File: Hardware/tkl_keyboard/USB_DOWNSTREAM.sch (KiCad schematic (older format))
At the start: 2 parts, among them J2 USB_C_Receptacle_USB2.0

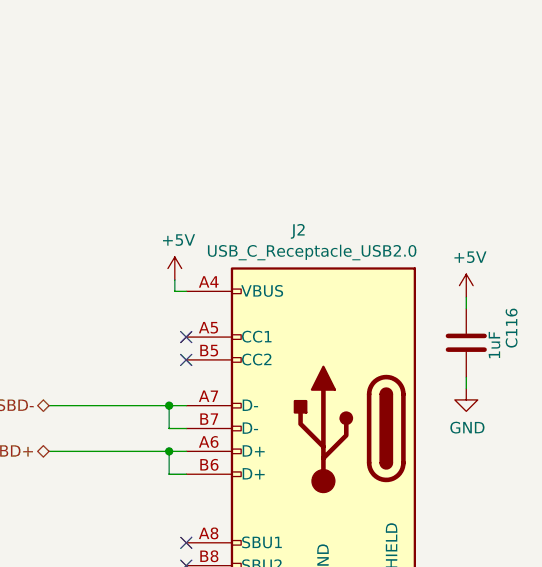
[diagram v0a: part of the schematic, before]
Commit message: Keyswitch, LED and diode placement done
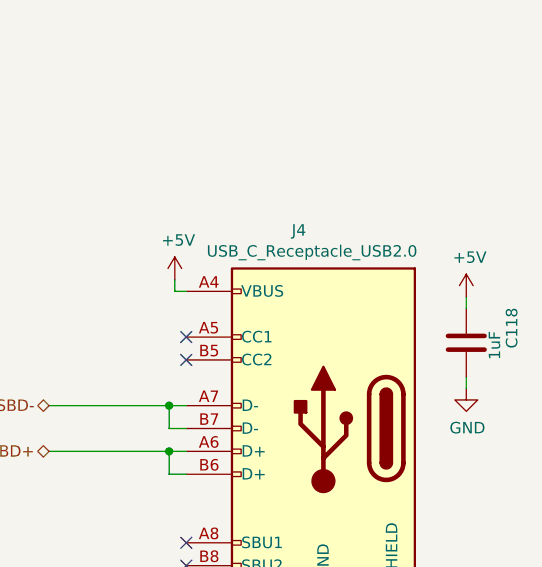
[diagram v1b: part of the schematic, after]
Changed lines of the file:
@@
 AR Path="/6511E0C5/651136DD" Ref="J3"  Part="1"
 AR Path="/65128D7D/651136DD" Ref="J4"  Part="1"
-F 0 "J2" H 6257 4567 50  0000 C CNN
+F 0 "J4" H 6257 4567 50  0000 C CNN
 F 1 "USB_C_Receptacle_USB2.0" H 6200 4475 50  0000 C CNN
 F 2 "Connector_USB:USB_C_Receptacle_GCT_USB4085" H 6300 3700 50  0001 C CNN
@@
 AR Path="/6511E0C5/651136EF" Ref="#PWR0497"  Part="1"
 AR Path="/65128D7D/651136EF" Ref="#PWR0501"  Part="1"
-F 0 "#PWR0493" H 6575 4425 50  0001 C CNN
+F 0 "#PWR0501" H 6575 4425 50  0001 C CNN
 F 1 "GND" H 6580 4502 50  0000 C CNN
 F 2 "" H 6575 4675 50  0001 C CNN
@@
 AR Path="/6511E0C5/651136FD" Ref="#PWR0496"  Part="1"
 AR Path="/65128D7D/651136FD" Ref="#PWR0500"  Part="1"
-F 0 "#PWR0492" H 5500 2900 50  0001 C CNN
+F 0 "#PWR0500" H 5500 2900 50  0001 C CNN
 F 1 "+5V" H 5515 3223 50  0000 C CNN
 F 2 "" H 5500 3050 50  0001 C CNN
@@
 AR Path="/6511E0C5/65113705" Ref="C117"  Part="1"
 AR Path="/65128D7D/65113705" Ref="C118"  Part="1"
-F 0 "C116" V 6975 3300 50  0000 L CNN
+F 0 "C118" V 6975 3300 50  0000 L CNN
 F 1 "1uF" V 6900 3250 50  0000 L CNN
 F 2 "Capacitor_smd:C_0603_1608Metric" H 6813 3175 50  0001 C CNN
@@
 AR Path="/6511E0C5/6511370B" Ref="#PWR0498"  Part="1"
 AR Path="/65128D7D/6511370B" Ref="#PWR0502"  Part="1"
-F 0 "#PWR0494" H 6775 2975 50  0001 C CNN
+F 0 "#PWR0502" H 6775 2975 50  0001 C CNN
 F 1 "+5V" H 6790 3298 50  0000 C CNN
 F 2 "" H 6775 3125 50  0001 C CNN
@@
 AR Path="/6511E0C5/65113712" Ref="#PWR0499"  Part="1"
 AR Path="/65128D7D/65113712" Ref="#PWR0503"  Part="1"
-F 0 "#PWR0495" H 6775 3275 50  0001 C CNN
+F 0 "#PWR0503" H 6775 3275 50  0001 C CNN
 F 1 "GND" H 6780 3352 50  0000 C CNN
 F 2 "" H 6775 3525 50  0001 C CNN

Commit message: LEDs and diodes routed
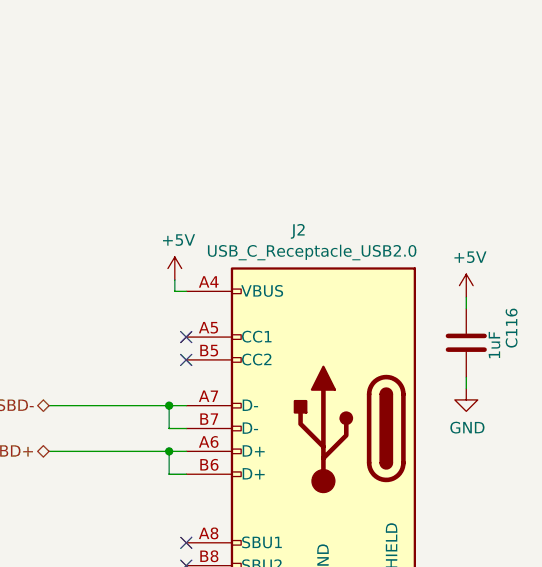
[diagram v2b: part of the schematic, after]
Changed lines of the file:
@@
 AR Path="/6511E0C5/651136DD" Ref="J3"  Part="1"
 AR Path="/65128D7D/651136DD" Ref="J4"  Part="1"
-F 0 "J4" H 6257 4567 50  0000 C CNN
+F 0 "J2" H 6257 4567 50  0000 C CNN
 F 1 "USB_C_Receptacle_USB2.0" H 6200 4475 50  0000 C CNN
 F 2 "Connector_USB:USB_C_Receptacle_GCT_USB4085" H 6300 3700 50  0001 C CNN
@@
 AR Path="/6511E0C5/65113705" Ref="C117"  Part="1"
 AR Path="/65128D7D/65113705" Ref="C118"  Part="1"
-F 0 "C118" V 6975 3300 50  0000 L CNN
+F 0 "C116" V 6975 3300 50  0000 L CNN
 F 1 "1uF" V 6900 3250 50  0000 L CNN
 F 2 "Capacitor_smd:C_0603_1608Metric" H 6813 3175 50  0001 C CNN

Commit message: Rows and columns routed to controller. Extended top board edge to fit OLED. Removed optional resistors around CMC.
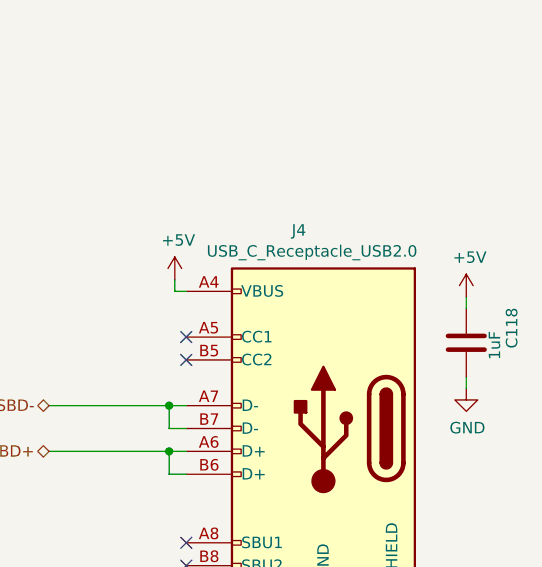
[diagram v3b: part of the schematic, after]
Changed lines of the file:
@@
 $Descr A4 11693 8268
 encoding utf-8
-Sheet 8 11
+Sheet 11 11
 Title ""
 Date ""
@@
 AR Path="/6511E0C5/651136DD" Ref="J3"  Part="1"
 AR Path="/65128D7D/651136DD" Ref="J4"  Part="1"
-F 0 "J2" H 6257 4567 50  0000 C CNN
+F 0 "J4" H 6257 4567 50  0000 C CNN
 F 1 "USB_C_Receptacle_USB2.0" H 6200 4475 50  0000 C CNN
 F 2 "Connector_USB:USB_C_Receptacle_GCT_USB4085" H 6300 3700 50  0001 C CNN
@@
 AR Path="/6511E0C5/65113705" Ref="C117"  Part="1"
 AR Path="/65128D7D/65113705" Ref="C118"  Part="1"
-F 0 "C116" V 6975 3300 50  0000 L CNN
+F 0 "C118" V 6975 3300 50  0000 L CNN
 F 1 "1uF" V 6900 3250 50  0000 L CNN
 F 2 "Capacitor_smd:C_0603_1608Metric" H 6813 3175 50  0001 C CNN

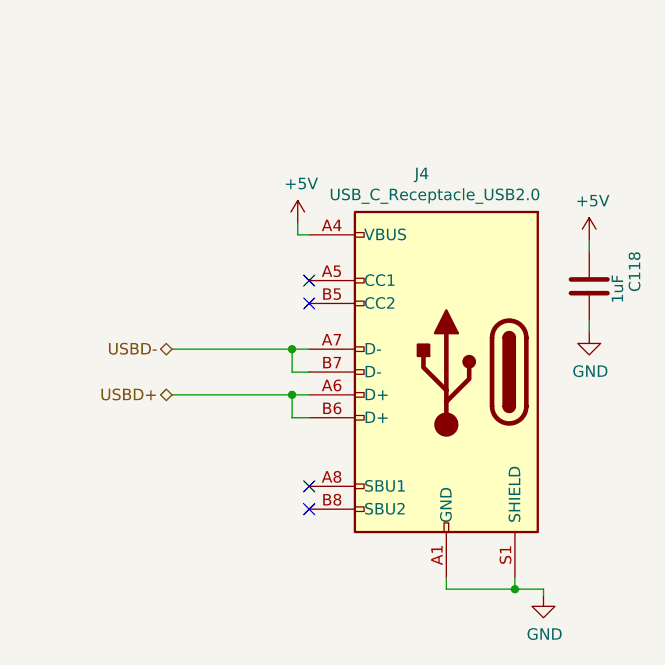
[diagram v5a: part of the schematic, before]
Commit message: Fixing USB circuit, adding data line resistors as per AN-5052
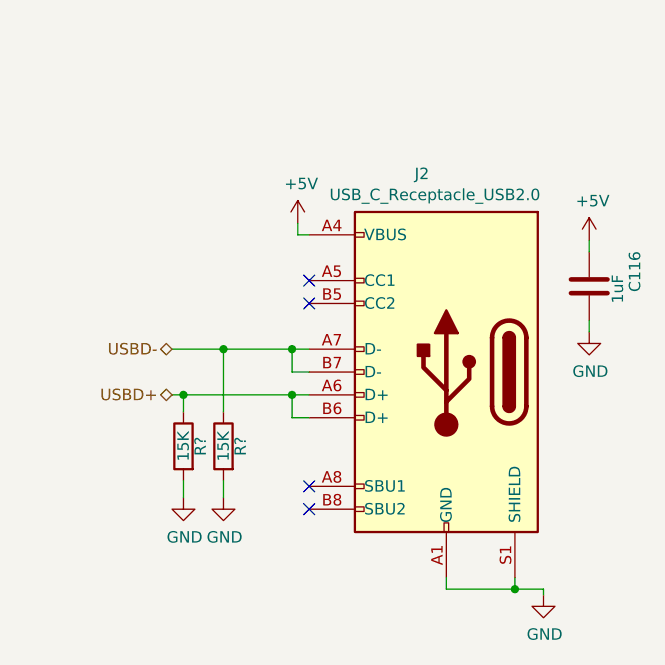
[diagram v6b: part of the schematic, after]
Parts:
- added R? (x2): 15K, resistor_smd:R_0603_1608Metric, symbol Device:R
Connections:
- net GND: now also R?.2, R?.2
- net USBD+: now also R?.1
- net USBD-: now also R?.1
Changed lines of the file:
@@
 $Descr A4 11693 8268
 encoding utf-8
-Sheet 11 12
+Sheet 8 12
 Title ""
 Date ""
@@
 AR Path="/6511E0C5/651136DD" Ref="J3"  Part="1"
 AR Path="/65128D7D/651136DD" Ref="J4"  Part="1"
-F 0 "J4" H 6257 4567 50  0000 C CNN
+F 0 "J2" H 6257 4567 50  0000 C CNN
 F 1 "USB_C_Receptacle_USB2.0" H 6200 4475 50  0000 C CNN
 F 2 "Connector_USB:USB_C_Receptacle_GCT_USB4085" H 6300 3700 50  0001 C CNN
@@
 	5475 3600 5550 3600
 Wire Wire Line
-	4950 3600 5475 3600
+	4950 3600 5175 3600
 Connection ~ 5475 3600
 Wire Wire Line
-	4950 3800 5475 3800
+	4950 3800 5000 3800
 Connection ~ 5475 3800
 NoConn ~ 5550 4200
@@
 AR Path="/6511E0C5/651136EF" Ref="#PWR0497"  Part="1"
 AR Path="/65128D7D/651136EF" Ref="#PWR0501"  Part="1"
-F 0 "#PWR0501" H 6575 4425 50  0001 C CNN
+F 0 "#PWR0493" H 6575 4425 50  0001 C CNN
 F 1 "GND" H 6580 4502 50  0000 C CNN
 F 2 "" H 6575 4675 50  0001 C CNN
@@
 AR Path="/6511E0C5/651136FD" Ref="#PWR0496"  Part="1"
 AR Path="/65128D7D/651136FD" Ref="#PWR0500"  Part="1"
-F 0 "#PWR0500" H 5500 2900 50  0001 C CNN
+F 0 "#PWR0492" H 5500 2900 50  0001 C CNN
 F 1 "+5V" H 5515 3223 50  0000 C CNN
 F 2 "" H 5500 3050 50  0001 C CNN
@@
 AR Path="/6511E0C5/65113705" Ref="C117"  Part="1"
 AR Path="/65128D7D/65113705" Ref="C118"  Part="1"
-F 0 "C118" V 6975 3300 50  0000 L CNN
+F 0 "C116" V 6975 3300 50  0000 L CNN
 F 1 "1uF" V 6900 3250 50  0000 L CNN
 F 2 "Capacitor_smd:C_0603_1608Metric" H 6813 3175 50  0001 C CNN
@@
 AR Path="/6511E0C5/6511370B" Ref="#PWR0498"  Part="1"
 AR Path="/65128D7D/6511370B" Ref="#PWR0502"  Part="1"
-F 0 "#PWR0502" H 6775 2975 50  0001 C CNN
+F 0 "#PWR0494" H 6775 2975 50  0001 C CNN
 F 1 "+5V" H 6790 3298 50  0000 C CNN
 F 2 "" H 6775 3125 50  0001 C CNN
@@
 AR Path="/6511E0C5/65113712" Ref="#PWR0499"  Part="1"
 AR Path="/65128D7D/65113712" Ref="#PWR0503"  Part="1"
-F 0 "#PWR0503" H 6775 3275 50  0001 C CNN
+F 0 "#PWR0495" H 6775 3275 50  0001 C CNN
 F 1 "GND" H 6780 3352 50  0000 C CNN
 F 2 "" H 6775 3525 50  0001 C CNN
@@
 Text HLabel 4950 3800 0    50   BiDi ~ 0
 USBD+
+$Comp
+L Device:R R?
+U 1 1 614BD77F
+P 5000 4025
+AR Path="/6114D32E/614BD77F" Ref="R?"  Part="1"
+AR Path="/6247A5CE/614BD77F" Ref="R?"  Part="1"
+AR Path="/61234350/614BD77F" Ref="R?"  Part="1"
+AR Path="/62FAC6FD/614BD77F" Ref="R?"  Part="1"
+AR Path="/650FF941/614BD77F" Ref="R?"  Part="1"
+AR Path="/6511E0C5/614BD77F" Ref="R?"  Part="1"
+AR Path="/65128D7D/614BD77F" Ref="R?"  Part="1"
+F 0 "R?" V 4925 4025 50  0000 C CNN
+F 1 "15K" V 5000 4025 50  0000 C CNN
+F 2 "resistor_smd:R_0603_1608Metric" V 4930 4025 50  0001 C CNN
+F 3 "~" H 5000 4025 50  0001 C CNN
+	1    5000 4025
+	-1   0    0    -1
+$EndComp
+$Comp
+L Device:R R?
+U 1 1 614BD896
+P 5175 4025
+AR Path="/6114D32E/614BD896" Ref="R?"  Part="1"
+AR Path="/6247A5CE/614BD896" Ref="R?"  Part="1"
+AR Path="/61234350/614BD896" Ref="R?"  Part="1"
+AR Path="/62FAC6FD/614BD896" Ref="R?"  Part="1"
+AR Path="/650FF941/614BD896" Ref="R?"  Part="1"
+AR Path="/6511E0C5/614BD896" Ref="R?"  Part="1"
+AR Path="/65128D7D/614BD896" Ref="R?"  Part="1"
+F 0 "R?" V 5100 4025 50  0000 C CNN
+F 1 "15K" V 5175 4025 50  0000 C CNN
+F 2 "resistor_smd:R_0603_1608Metric" V 5105 4025 50  0001 C CNN
+F 3 "~" H 5175 4025 50  0001 C CNN
+	1    5175 4025
+	-1   0    0    -1
+$EndComp
+Wire Wire Line
+	5000 3875 5000 3800
+Connection ~ 5000 3800
+Wire Wire Line
+	5000 3800 5475 3800
+Wire Wire Line
+	5175 3875 5175 3600
+Connection ~ 5175 3600
+Wire Wire Line
+	5175 3600 5475 3600
+$Comp
+L power:GND #PWR?
+U 1 1 614BE05C
+P 5000 4250
+AR Path="/6114D32E/614BE05C" Ref="#PWR?"  Part="1"
+AR Path="/6247A5CE/614BE05C" Ref="#PWR?"  Part="1"
+AR Path="/61234350/614BE05C" Ref="#PWR?"  Part="1"
+AR Path="/62FAC6FD/614BE05C" Ref="#PWR?"  Part="1"
+AR Path="/650FF941/614BE05C" Ref="#PWR?"  Part="1"
+AR Path="/6511E0C5/614BE05C" Ref="#PWR?"  Part="1"
+AR Path="/65128D7D/614BE05C" Ref="#PWR?"  Part="1"
+F 0 "#PWR?" H 5000 4000 50  0001 C CNN
+F 1 "GND" H 5005 4077 50  0000 C CNN
+F 2 "" H 5000 4250 50  0001 C CNN
+F 3 "" H 5000 4250 50  0001 C CNN
+	1    5000 4250
+	1    0    0    -1
+$EndComp
+$Comp
+L power:GND #PWR?
+U 1 1 614BE37F
+P 5175 4250
+AR Path="/6114D32E/614BE37F" Ref="#PWR?"  Part="1"
+AR Path="/6247A5CE/614BE37F" Ref="#PWR?"  Part="1"
+AR Path="/61234350/614BE37F" Ref="#PWR?"  Part="1"
+AR Path="/62FAC6FD/614BE37F" Ref="#PWR?"  Part="1"
+AR Path="/650FF941/614BE37F" Ref="#PWR?"  Part="1"
+AR Path="/6511E0C5/614BE37F" Ref="#PWR?"  Part="1"
+AR Path="/65128D7D/614BE37F" Ref="#PWR?"  Part="1"
+F 0 "#PWR?" H 5175 4000 50  0001 C CNN
+F 1 "GND" H 5180 4077 50  0000 C CNN
+F 2 "" H 5175 4250 50  0001 C CNN
+F 3 "" H 5175 4250 50  0001 C CNN
+	1    5175 4250
+	1    0    0    -1
+$EndComp
+Wire Wire Line
+	5000 4250 5000 4175
+Wire Wire Line
+	5175 4250 5175 4175
 $EndSCHEMATC

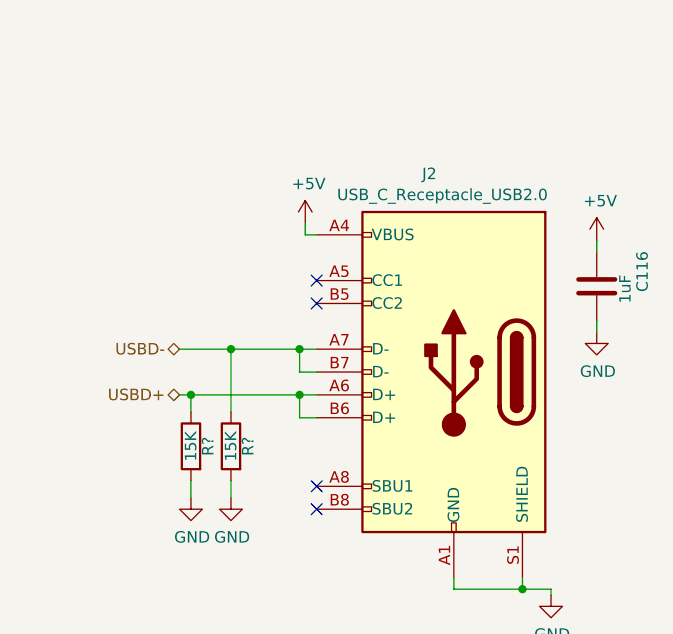
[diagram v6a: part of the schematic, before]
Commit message: Tidying schematic
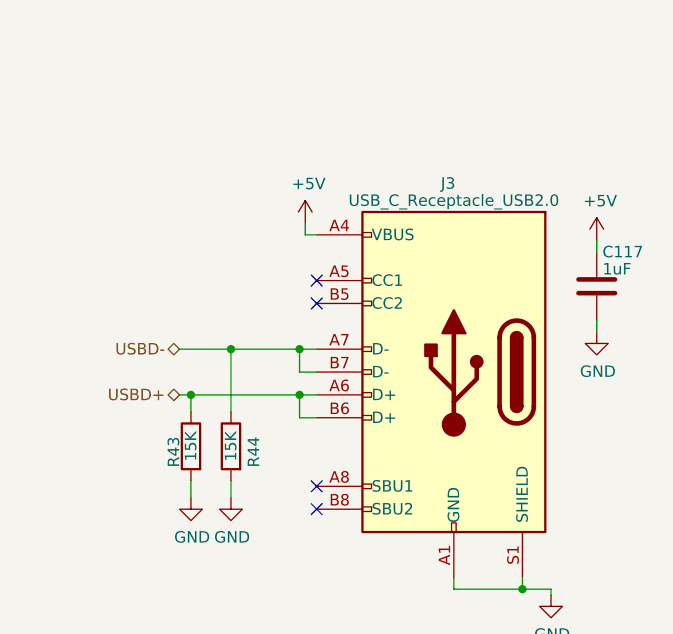
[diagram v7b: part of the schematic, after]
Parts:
- gave numbers to parts that had none: 2
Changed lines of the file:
@@
 $Descr A4 11693 8268
 encoding utf-8
-Sheet 8 12
-Title ""
+Sheet 10 12
+Title "TKL Keyboard"
 Date ""
-Rev ""
+Rev "0"
 Comp ""
 Comment1 ""
@@
 AR Path="/6511E0C5/651136DD" Ref="J3"  Part="1"
 AR Path="/65128D7D/651136DD" Ref="J4"  Part="1"
-F 0 "J2" H 6257 4567 50  0000 C CNN
-F 1 "USB_C_Receptacle_USB2.0" H 6200 4475 50  0000 C CNN
+F 0 "J3" H 6175 4525 50  0000 C CNN
+F 1 "USB_C_Receptacle_USB2.0" H 6150 4450 50  0000 C CNN
 F 2 "Connector_USB:USB_C_Receptacle_GCT_USB4085" H 6300 3700 50  0001 C CNN
 F 3 "https://www.usb.org/sites/default/files/documents/usb_type-c.zip" H 6300 3700 50  0001 C CNN
@@
 AR Path="/6511E0C5/651136EF" Ref="#PWR0497"  Part="1"
 AR Path="/65128D7D/651136EF" Ref="#PWR0501"  Part="1"
-F 0 "#PWR0493" H 6575 4425 50  0001 C CNN
+F 0 "#PWR0497" H 6575 4425 50  0001 C CNN
 F 1 "GND" H 6580 4502 50  0000 C CNN
 F 2 "" H 6575 4675 50  0001 C CNN
@@
 AR Path="/6511E0C5/651136FD" Ref="#PWR0496"  Part="1"
 AR Path="/65128D7D/651136FD" Ref="#PWR0500"  Part="1"
-F 0 "#PWR0492" H 5500 2900 50  0001 C CNN
+F 0 "#PWR0496" H 5500 2900 50  0001 C CNN
 F 1 "+5V" H 5515 3223 50  0000 C CNN
 F 2 "" H 5500 3050 50  0001 C CNN
@@
 AR Path="/6511E0C5/65113705" Ref="C117"  Part="1"
 AR Path="/65128D7D/65113705" Ref="C118"  Part="1"
-F 0 "C116" V 6975 3300 50  0000 L CNN
-F 1 "1uF" V 6900 3250 50  0000 L CNN
+F 0 "C117" H 6800 3475 50  0000 L CNN
+F 1 "1uF" H 6800 3400 50  0000 L CNN
 F 2 "Capacitor_smd:C_0603_1608Metric" H 6813 3175 50  0001 C CNN
 F 3 "~" H 6775 3325 50  0001 C CNN
@@
 AR Path="/6511E0C5/6511370B" Ref="#PWR0498"  Part="1"
 AR Path="/65128D7D/6511370B" Ref="#PWR0502"  Part="1"
-F 0 "#PWR0494" H 6775 2975 50  0001 C CNN
+F 0 "#PWR0498" H 6775 2975 50  0001 C CNN
 F 1 "+5V" H 6790 3298 50  0000 C CNN
 F 2 "" H 6775 3125 50  0001 C CNN
@@
 AR Path="/6511E0C5/65113712" Ref="#PWR0499"  Part="1"
 AR Path="/65128D7D/65113712" Ref="#PWR0503"  Part="1"
-F 0 "#PWR0495" H 6775 3275 50  0001 C CNN
+F 0 "#PWR0499" H 6775 3275 50  0001 C CNN
 F 1 "GND" H 6780 3352 50  0000 C CNN
 F 2 "" H 6775 3525 50  0001 C CNN
@@
 AR Path="/61234350/614BD77F" Ref="R?"  Part="1"
 AR Path="/62FAC6FD/614BD77F" Ref="R?"  Part="1"
-AR Path="/650FF941/614BD77F" Ref="R?"  Part="1"
-AR Path="/6511E0C5/614BD77F" Ref="R?"  Part="1"
-AR Path="/65128D7D/614BD77F" Ref="R?"  Part="1"
-F 0 "R?" V 4925 4025 50  0000 C CNN
+AR Path="/650FF941/614BD77F" Ref="R40"  Part="1"
+AR Path="/6511E0C5/614BD77F" Ref="R43"  Part="1"
+AR Path="/65128D7D/614BD77F" Ref="R45"  Part="1"
+F 0 "R43" V 5075 4000 50  0000 C CNN
 F 1 "15K" V 5000 4025 50  0000 C CNN
 F 2 "resistor_smd:R_0603_1608Metric" V 4930 4025 50  0001 C CNN
@@
 AR Path="/61234350/614BD896" Ref="R?"  Part="1"
 AR Path="/62FAC6FD/614BD896" Ref="R?"  Part="1"
-AR Path="/650FF941/614BD896" Ref="R?"  Part="1"
-AR Path="/6511E0C5/614BD896" Ref="R?"  Part="1"
-AR Path="/65128D7D/614BD896" Ref="R?"  Part="1"
-F 0 "R?" V 5100 4025 50  0000 C CNN
+AR Path="/650FF941/614BD896" Ref="R41"  Part="1"
+AR Path="/6511E0C5/614BD896" Ref="R44"  Part="1"
+AR Path="/65128D7D/614BD896" Ref="R46"  Part="1"
+F 0 "R44" V 5075 4000 50  0000 C CNN
 F 1 "15K" V 5175 4025 50  0000 C CNN
 F 2 "resistor_smd:R_0603_1608Metric" V 5105 4025 50  0001 C CNN
@@
 AR Path="/61234350/614BE05C" Ref="#PWR?"  Part="1"
 AR Path="/62FAC6FD/614BE05C" Ref="#PWR?"  Part="1"
-AR Path="/650FF941/614BE05C" Ref="#PWR?"  Part="1"
-AR Path="/6511E0C5/614BE05C" Ref="#PWR?"  Part="1"
-AR Path="/65128D7D/614BE05C" Ref="#PWR?"  Part="1"
-F 0 "#PWR?" H 5000 4000 50  0001 C CNN
+AR Path="/650FF941/614BE05C" Ref="#PWR0536"  Part="1"
+AR Path="/6511E0C5/614BE05C" Ref="#PWR0539"  Part="1"
+AR Path="/65128D7D/614BE05C" Ref="#PWR0541"  Part="1"
+F 0 "#PWR0539" H 5000 4000 50  0001 C CNN
 F 1 "GND" H 5005 4077 50  0000 C CNN
 F 2 "" H 5000 4250 50  0001 C CNN
@@
 AR Path="/61234350/614BE37F" Ref="#PWR?"  Part="1"
 AR Path="/62FAC6FD/614BE37F" Ref="#PWR?"  Part="1"
-AR Path="/650FF941/614BE37F" Ref="#PWR?"  Part="1"
-AR Path="/6511E0C5/614BE37F" Ref="#PWR?"  Part="1"
-AR Path="/65128D7D/614BE37F" Ref="#PWR?"  Part="1"
-F 0 "#PWR?" H 5175 4000 50  0001 C CNN
+AR Path="/650FF941/614BE37F" Ref="#PWR0537"  Part="1"
+AR Path="/6511E0C5/614BE37F" Ref="#PWR0540"  Part="1"
+AR Path="/65128D7D/614BE37F" Ref="#PWR0542"  Part="1"
+F 0 "#PWR0540" H 5175 4000 50  0001 C CNN
 F 1 "GND" H 5180 4077 50  0000 C CNN
 F 2 "" H 5175 4250 50  0001 C CNN

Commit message: Generating gerbers
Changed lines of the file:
@@
 AR Path="/6511E0C5/651136DD" Ref="J3"  Part="1"
 AR Path="/65128D7D/651136DD" Ref="J4"  Part="1"
-F 0 "J3" H 6175 4525 50  0000 C CNN
+F 0 "J4" H 6175 4525 50  0000 C CNN
 F 1 "USB_C_Receptacle_USB2.0" H 6150 4450 50  0000 C CNN
 F 2 "Connector_USB:USB_C_Receptacle_GCT_USB4085" H 6300 3700 50  0001 C CNN
@@
 AR Path="/6511E0C5/651136EF" Ref="#PWR0497"  Part="1"
 AR Path="/65128D7D/651136EF" Ref="#PWR0501"  Part="1"
-F 0 "#PWR0497" H 6575 4425 50  0001 C CNN
+F 0 "#PWR0501" H 6575 4425 50  0001 C CNN
 F 1 "GND" H 6580 4502 50  0000 C CNN
 F 2 "" H 6575 4675 50  0001 C CNN
@@
 AR Path="/6511E0C5/651136FD" Ref="#PWR0496"  Part="1"
 AR Path="/65128D7D/651136FD" Ref="#PWR0500"  Part="1"
-F 0 "#PWR0496" H 5500 2900 50  0001 C CNN
+F 0 "#PWR0500" H 5500 2900 50  0001 C CNN
 F 1 "+5V" H 5515 3223 50  0000 C CNN
 F 2 "" H 5500 3050 50  0001 C CNN
@@
 AR Path="/6511E0C5/65113705" Ref="C117"  Part="1"
 AR Path="/65128D7D/65113705" Ref="C118"  Part="1"
-F 0 "C117" H 6800 3475 50  0000 L CNN
+F 0 "C118" H 6800 3475 50  0000 L CNN
 F 1 "1uF" H 6800 3400 50  0000 L CNN
 F 2 "Capacitor_smd:C_0603_1608Metric" H 6813 3175 50  0001 C CNN
@@
 AR Path="/6511E0C5/6511370B" Ref="#PWR0498"  Part="1"
 AR Path="/65128D7D/6511370B" Ref="#PWR0502"  Part="1"
-F 0 "#PWR0498" H 6775 2975 50  0001 C CNN
+F 0 "#PWR0502" H 6775 2975 50  0001 C CNN
 F 1 "+5V" H 6790 3298 50  0000 C CNN
 F 2 "" H 6775 3125 50  0001 C CNN
@@
 AR Path="/6511E0C5/65113712" Ref="#PWR0499"  Part="1"
 AR Path="/65128D7D/65113712" Ref="#PWR0503"  Part="1"
-F 0 "#PWR0499" H 6775 3275 50  0001 C CNN
+F 0 "#PWR0503" H 6775 3275 50  0001 C CNN
 F 1 "GND" H 6780 3352 50  0000 C CNN
 F 2 "" H 6775 3525 50  0001 C CNN
@@
 AR Path="/6511E0C5/614BD77F" Ref="R43"  Part="1"
 AR Path="/65128D7D/614BD77F" Ref="R45"  Part="1"
-F 0 "R43" V 5075 4000 50  0000 C CNN
+F 0 "R45" V 5075 4000 50  0000 C CNN
 F 1 "15K" V 5000 4025 50  0000 C CNN
 F 2 "resistor_smd:R_0603_1608Metric" V 4930 4025 50  0001 C CNN
@@
 AR Path="/6511E0C5/614BD896" Ref="R44"  Part="1"
 AR Path="/65128D7D/614BD896" Ref="R46"  Part="1"
-F 0 "R44" V 5075 4000 50  0000 C CNN
+F 0 "R46" V 5075 4000 50  0000 C CNN
 F 1 "15K" V 5175 4025 50  0000 C CNN
 F 2 "resistor_smd:R_0603_1608Metric" V 5105 4025 50  0001 C CNN
@@
 AR Path="/6511E0C5/614BE05C" Ref="#PWR0539"  Part="1"
 AR Path="/65128D7D/614BE05C" Ref="#PWR0541"  Part="1"
-F 0 "#PWR0539" H 5000 4000 50  0001 C CNN
+F 0 "#PWR0541" H 5000 4000 50  0001 C CNN
 F 1 "GND" H 5005 4077 50  0000 C CNN
 F 2 "" H 5000 4250 50  0001 C CNN
@@
 AR Path="/6511E0C5/614BE37F" Ref="#PWR0540"  Part="1"
 AR Path="/65128D7D/614BE37F" Ref="#PWR0542"  Part="1"
-F 0 "#PWR0540" H 5175 4000 50  0001 C CNN
+F 0 "#PWR0542" H 5175 4000 50  0001 C CNN
 F 1 "GND" H 5180 4077 50  0000 C CNN
 F 2 "" H 5175 4250 50  0001 C CNN
